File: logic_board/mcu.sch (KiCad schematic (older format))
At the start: 20 parts, among them J1 SWD, J6 Serial, SW1 TL3315NF160Q, SW2 TL3315NF160Q, SW3 TL3315NF160Q, SW4 TL3315NF160Q, U1 STM32G474CET6, Y1 8 MHz

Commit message: Remove external pullups.
The chip already has internal ones.
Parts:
- removed R1, R2, R4, R5: 10k, Resistors_SMD:R_0402, symbol Device:R
- removed R3: 100k, Resistors_SMD:R_0402, symbol Device:R
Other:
- moved on the sheet: SW1, SW2, SW3, SW4
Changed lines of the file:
@@
 	7900 5200 8000 5200
-$Comp
-L Device:R R3
-U 1 1 5E3A1553
-P 7250 4500
-F 0 "R3" H 7320 4546 50  0000 L CNN
-F 1 "100k" H 7320 4455 50  0000 L CNN
-F 2 "Resistors_SMD:R_0402" V 7180 4500 50  0001 C CNN
-F 3 "~" H 7250 4500 50  0001 C CNN
-	1    7250 4500
-	1    0    0    -1
-$EndComp
-$Comp
-L power:+3V3 #PWR09
-U 1 1 5E3A1C59
-P 7250 4150
-F 0 "#PWR09" H 7250 4000 50  0001 C CNN
-F 1 "+3V3" H 7265 4323 50  0000 C CNN
-F 2 "" H 7250 4150 50  0001 C CNN
-F 3 "" H 7250 4150 50  0001 C CNN
-	1    7250 4150
-	1    0    0    -1
-$EndComp
-Wire Wire Line
-	7250 4150 7250 4350
-Wire Wire Line
-	7250 4900 7250 4650
 $Comp
 L power:+3V3 #PWR010
@@
 	7800 5100 8000 5100
 Wire Wire Line
-	9600 1750 9700 1750
-Wire Wire Line
-	9600 2850 9700 2850
-Wire Wire Line
-	9700 2850 9700 2950
-Wire Wire Line
-	9700 1750 9700 2150
-Connection ~ 9700 2850
-Wire Wire Line
-	7750 1750 8150 1750
-Wire Wire Line
-	9600 2150 9700 2150
-Connection ~ 9700 2150
-Wire Wire Line
-	9700 2150 9700 2500
-Wire Wire Line
-	9600 2500 9700 2500
-Connection ~ 9700 2500
-Wire Wire Line
-	9700 2500 9700 2850
-$Comp
-L Device:R R1
-U 1 1 5E46297B
-P 8150 1400
-F 0 "R1" H 8220 1446 50  0000 L CNN
-F 1 "10k" H 8220 1355 50  0000 L CNN
-F 2 "Resistors_SMD:R_0402" V 8080 1400 50  0001 C CNN
-F 3 "~" H 8150 1400 50  0001 C CNN
-	1    8150 1400
-	1    0    0    -1
-$EndComp
-$Comp
-L Device:R R2
-U 1 1 5E463893
-P 8400 1400
-F 0 "R2" H 8470 1446 50  0000 L CNN
-F 1 "10k" H 8470 1355 50  0000 L CNN
-F 2 "Resistors_SMD:R_0402" V 8330 1400 50  0001 C CNN
-F 3 "~" H 8400 1400 50  0001 C CNN
-	1    8400 1400
-	1    0    0    -1
-$EndComp
-$Comp
-L Device:R R4
-U 1 1 5E463D11
-P 8650 1400
-F 0 "R4" H 8720 1446 50  0000 L CNN
-F 1 "10k" H 8720 1355 50  0000 L CNN
-F 2 "Resistors_SMD:R_0402" V 8580 1400 50  0001 C CNN
-F 3 "~" H 8650 1400 50  0001 C CNN
-	1    8650 1400
-	1    0    0    -1
-$EndComp
-$Comp
-L Device:R R5
-U 1 1 5E4642B0
-P 8900 1400
-F 0 "R5" H 8970 1446 50  0000 L CNN
-F 1 "10k" H 8970 1355 50  0000 L CNN
-F 2 "Resistors_SMD:R_0402" V 8830 1400 50  0001 C CNN
-F 3 "~" H 8900 1400 50  0001 C CNN
-	1    8900 1400
-	1    0    0    -1
-$EndComp
-Wire Wire Line
-	8150 1550 8150 1750
-Connection ~ 8150 1750
-Wire Wire Line
-	8400 1550 8400 2150
-Connection ~ 8400 2150
-Wire Wire Line
-	8650 1550 8650 2500
-Connection ~ 8650 2500
-Wire Wire Line
-	8900 1550 8900 2850
-Connection ~ 8900 2850
-$Comp
-L power:+3V3 #PWR08
-U 1 1 5E46F451
-P 8150 1000
-F 0 "#PWR08" H 8150 850 50  0001 C CNN
-F 1 "+3V3" H 8165 1173 50  0000 C CNN
-F 2 "" H 8150 1000 50  0001 C CNN
-F 3 "" H 8150 1000 50  0001 C CNN
-	1    8150 1000
-	1    0    0    -1
-$EndComp
-Wire Wire Line
-	8900 1250 8900 1100
-Wire Wire Line
-	8900 1100 8650 1100
-Wire Wire Line
-	8150 1100 8150 1000
-Wire Wire Line
-	8150 1250 8150 1100
-Connection ~ 8150 1100
-Wire Wire Line
-	8400 1250 8400 1100
-Connection ~ 8400 1100
-Wire Wire Line
-	8400 1100 8150 1100
-Wire Wire Line
-	8650 1250 8650 1100
-Connection ~ 8650 1100
-Wire Wire Line
-	8650 1100 8400 1100
+	9700 2000 9800 2000
+Wire Wire Line
+	9700 3100 9800 3100
+Wire Wire Line
+	9800 3100 9800 3200
+Wire Wire Line
+	9800 2000 9800 2400
+Connection ~ 9800 3100
+Wire Wire Line
+	9700 2400 9800 2400
+Connection ~ 9800 2400
+Wire Wire Line
+	9800 2400 9800 2750
+Wire Wire Line
+	9700 2750 9800 2750
+Connection ~ 9800 2750
+Wire Wire Line
+	9800 2750 9800 3100
 Text GLabel 6400 4800 2    50   BiDi ~ 0
 USB_DP
@@
 L Switch:SW_Push SW4
 U 1 1 5E4374E4
-P 9400 2850
-F 0 "SW4" H 9400 3135 50  0000 C CNN
-F 1 "TL3315NF160Q" H 9400 3044 50  0000 C CNN
-F 2 "custom_footprints:TL3315NF160Q_Tactile_Switch" H 9400 3050 50  0001 C CNN
-F 3 "http://spec_sheets.e-switch.com/specs/P010337.pdf" H 9400 3050 50  0001 C CNN
-F 4 "Switch Effect" H 9750 2950 50  0000 C CNN "Name"
-	1    9400 2850
+P 9500 3100
+F 0 "SW4" H 9500 3385 50  0000 C CNN
+F 1 "TL3315NF160Q" H 9500 3294 50  0000 C CNN
+F 2 "custom_footprints:TL3315NF160Q_Tactile_Switch" H 9500 3300 50  0001 C CNN
+F 3 "http://spec_sheets.e-switch.com/specs/P010337.pdf" H 9500 3300 50  0001 C CNN
+F 4 "Switch Effect" H 9850 3200 50  0000 C CNN "Name"
+	1    9500 3100
 	1    0    0    -1
 $EndComp
@@
 L Switch:SW_Push SW1
 U 1 1 5E437998
-P 9400 1750
-F 0 "SW1" H 9400 2035 50  0000 C CNN
-F 1 "TL3315NF160Q" H 9400 1944 50  0000 C CNN
-F 2 "custom_footprints:TL3315NF160Q_Tactile_Switch" H 9400 1950 50  0001 C CNN
-F 3 "http://spec_sheets.e-switch.com/specs/P010337.pdf" H 9400 1950 50  0001 C CNN
-F 4 "Volume Down" H 9750 1850 50  0000 C CNN "Name"
-	1    9400 1750
+P 9500 2000
+F 0 "SW1" H 9500 2285 50  0000 C CNN
+F 1 "TL3315NF160Q" H 9500 2194 50  0000 C CNN
+F 2 "custom_footprints:TL3315NF160Q_Tactile_Switch" H 9500 2200 50  0001 C CNN
+F 3 "http://spec_sheets.e-switch.com/specs/P010337.pdf" H 9500 2200 50  0001 C CNN
+F 4 "Volume Down" H 9850 2100 50  0000 C CNN "Name"
+	1    9500 2000
 	1    0    0    -1
 $EndComp
@@
 L Switch:SW_Push SW3
 U 1 1 5E436F53
-P 9400 2500
-F 0 "SW3" H 9400 2785 50  0000 C CNN
-F 1 "TL3315NF160Q" H 9400 2694 50  0000 C CNN
-F 2 "custom_footprints:TL3315NF160Q_Tactile_Switch" H 9400 2700 50  0001 C CNN
-F 3 "http://spec_sheets.e-switch.com/specs/P010337.pdf" H 9400 2700 50  0001 C CNN
-F 4 "Metronome" H 9700 2550 50  0000 C CNN "Name"
-	1    9400 2500
+P 9500 2750
+F 0 "SW3" H 9500 3035 50  0000 C CNN
+F 1 "TL3315NF160Q" H 9500 2944 50  0000 C CNN
+F 2 "custom_footprints:TL3315NF160Q_Tactile_Switch" H 9500 2950 50  0001 C CNN
+F 3 "http://spec_sheets.e-switch.com/specs/P010337.pdf" H 9500 2950 50  0001 C CNN
+F 4 "Metronome" H 9800 2800 50  0000 C CNN "Name"
+	1    9500 2750
 	1    0    0    -1
 $EndComp
@@
 L Switch:SW_Push SW2
 U 1 1 5E43625B
-P 9400 2150
-F 0 "SW2" H 9400 2435 50  0000 C CNN
-F 1 "TL3315NF160Q" H 9400 2344 50  0000 C CNN
-F 2 "custom_footprints:TL3315NF160Q_Tactile_Switch" H 9400 2350 50  0001 C CNN
-F 3 "http://spec_sheets.e-switch.com/specs/P010337.pdf" H 9400 2350 50  0001 C CNN
-F 4 "Volume Up" H 9800 2250 50  0000 C CNN "Field4"
-	1    9400 2150
+P 9500 2400
+F 0 "SW2" H 9500 2685 50  0000 C CNN
+F 1 "TL3315NF160Q" H 9500 2594 50  0000 C CNN
+F 2 "custom_footprints:TL3315NF160Q_Tactile_Switch" H 9500 2600 50  0001 C CNN
+F 3 "http://spec_sheets.e-switch.com/specs/P010337.pdf" H 9500 2600 50  0001 C CNN
+F 4 "Volume Up" H 9900 2500 50  0000 C CNN "Field4"
+	1    9500 2400
 	1    0    0    -1
 $EndComp
@@
 L power:GND #PWR0101
 U 1 1 5E31F2DC
-P 9700 2950
-F 0 "#PWR0101" H 9700 2700 50  0001 C CNN
-F 1 "GND" H 9705 2777 50  0000 C CNN
-F 2 "" H 9700 2950 50  0001 C CNN
-F 3 "" H 9700 2950 50  0001 C CNN
-	1    9700 2950
-	1    0    0    -1
-$EndComp
-Wire Wire Line
-	8150 1750 9200 1750
-Wire Wire Line
-	8400 2150 9200 2150
-Wire Wire Line
-	8650 2500 9200 2500
-Wire Wire Line
-	8900 2850 9200 2850
+P 9800 3200
+F 0 "#PWR0101" H 9800 2950 50  0001 C CNN
+F 1 "GND" H 9805 3027 50  0000 C CNN
+F 2 "" H 9800 3200 50  0001 C CNN
+F 3 "" H 9800 3200 50  0001 C CNN
+	1    9800 3200
+	1    0    0    -1
+$EndComp
 NoConn ~ 5300 2200
 Wire Wire Line
@@
 Text GLabel 4550 4300 0    50   Input ~ 0
 SW1
-Text GLabel 7750 1750 0    50   Input ~ 0
+Text GLabel 7850 2000 0    50   Input ~ 0
 SW1
-Text GLabel 7750 2150 0    50   Input ~ 0
+Text GLabel 7850 2400 0    50   Input ~ 0
 SW2
-Text GLabel 7750 2500 0    50   Input ~ 0
+Text GLabel 7850 2750 0    50   Input ~ 0
 SW3
-Text GLabel 7750 2850 0    50   Input ~ 0
+Text GLabel 7850 3100 0    50   Input ~ 0
 SW4
-Wire Wire Line
-	7750 2150 8400 2150
-Wire Wire Line
-	7750 2500 8650 2500
-Wire Wire Line
-	7750 2850 8900 2850
 Text GLabel 4550 3050 0    50   Input ~ 0
 SW2
@@
 	1    0    0    -1
 $EndComp
-Wire Wire Line
-	6150 4900 7250 4900
 Text Notes 8300 5000 0    50   ~ 0
 SWDIO
@@
 	6150 4500 6400 4500
 Wire Wire Line
-	7250 4900 7550 4900
-Wire Wire Line
 	7550 4900 7550 5000
 Wire Wire Line
 	7550 5000 8000 5000
-Connection ~ 7250 4900
 Wire Wire Line
 	6150 5000 7450 5000
@@
 Wire Wire Line
 	3650 4700 3800 4700
+Wire Wire Line
+	7850 2000 9300 2000
+Wire Wire Line
+	7850 2400 9300 2400
+Wire Wire Line
+	7850 2750 9300 2750
+Wire Wire Line
+	7850 3100 9300 3100
+Wire Wire Line
+	6150 4900 7550 4900
 $EndSCHEMATC

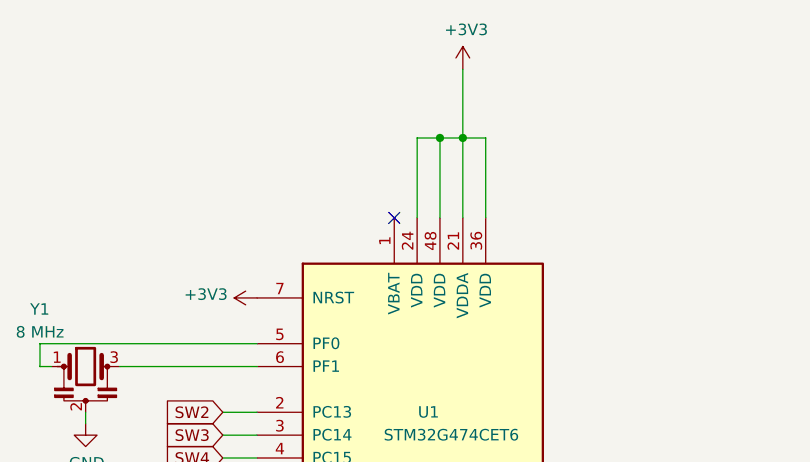
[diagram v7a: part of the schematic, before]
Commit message: Connect VBAT to VDD
From AN5096, "If no external battery is used in the application, it is recommended
to connect VBAT externally to VDD."
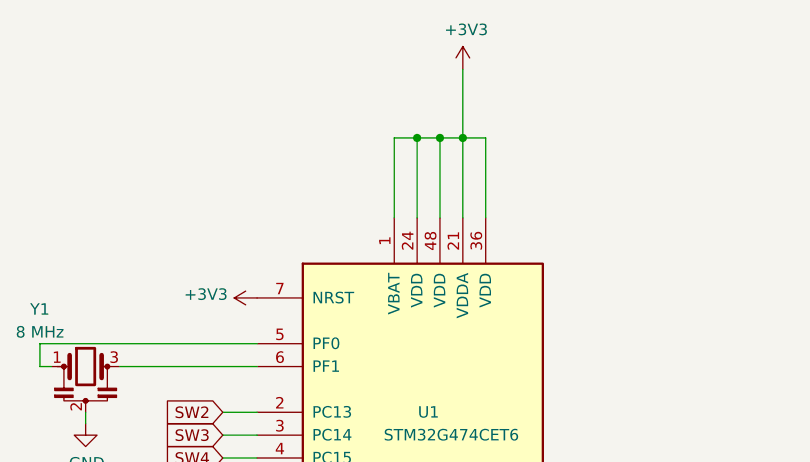
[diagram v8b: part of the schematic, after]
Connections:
- net +3V3: now also U1.1 (VBAT)
- no-connect marks 17 -> 16
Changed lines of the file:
@@
 	1    0    0    -1
 $EndComp
-NoConn ~ 5300 2200
 Wire Wire Line
 	5600 1850 5600 1550
@@
 Wire Wire Line
 	6150 4900 7550 4900
+Wire Wire Line
+	5400 1850 5300 1850
+Wire Wire Line
+	5300 1850 5300 2200
+Connection ~ 5400 1850
 $EndSCHEMATC
